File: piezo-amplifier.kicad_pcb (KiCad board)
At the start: 2 copper layers, 37 x 108 mm, 62 parts, among them J1 AudioJack4, J2 AudioJack4, J3 AudioJack4, J4 AudioJack4, J5 Conn_01x03_Male, J6 Conn_02x05_Odd_Even, SW1 734-7081, SW2 734-7081, U1 NE5532, U2 NE5532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

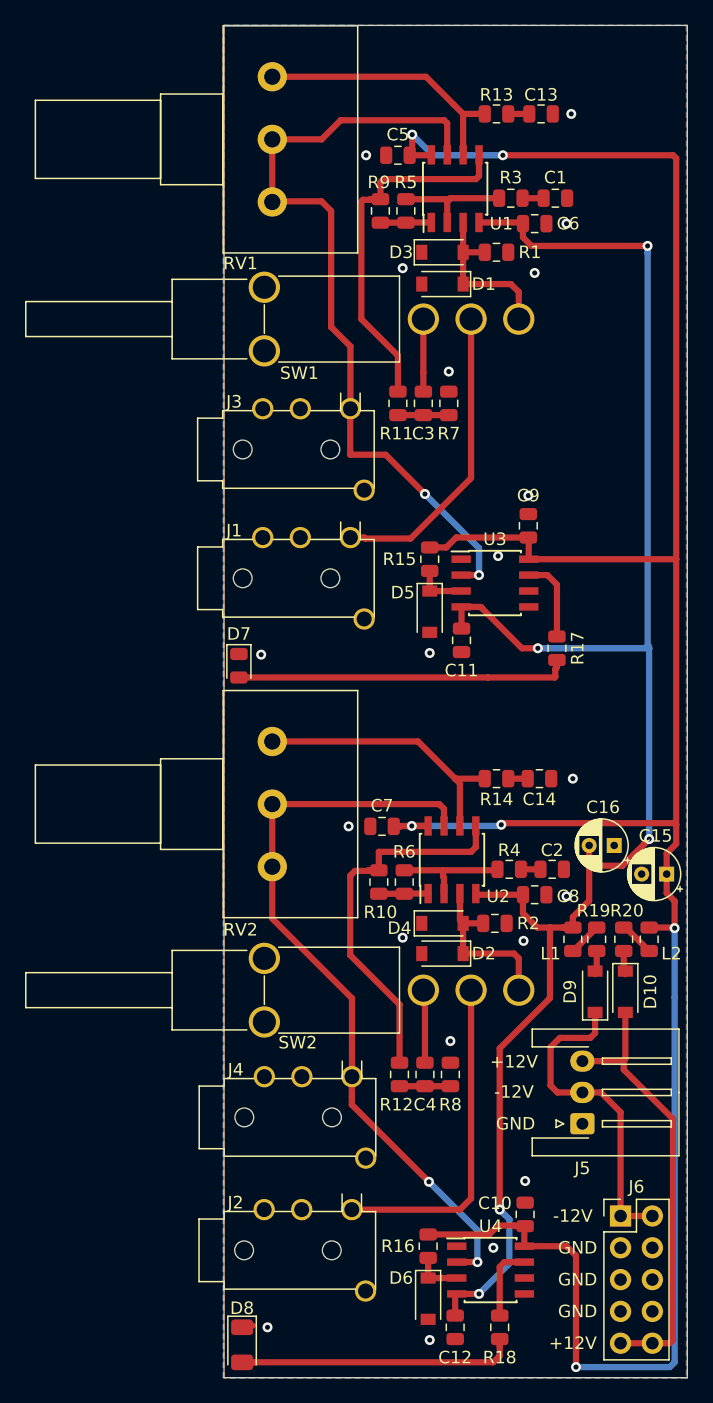
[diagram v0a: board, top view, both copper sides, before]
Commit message: switched to SMD capacitors, minor layout and silkscreen changes
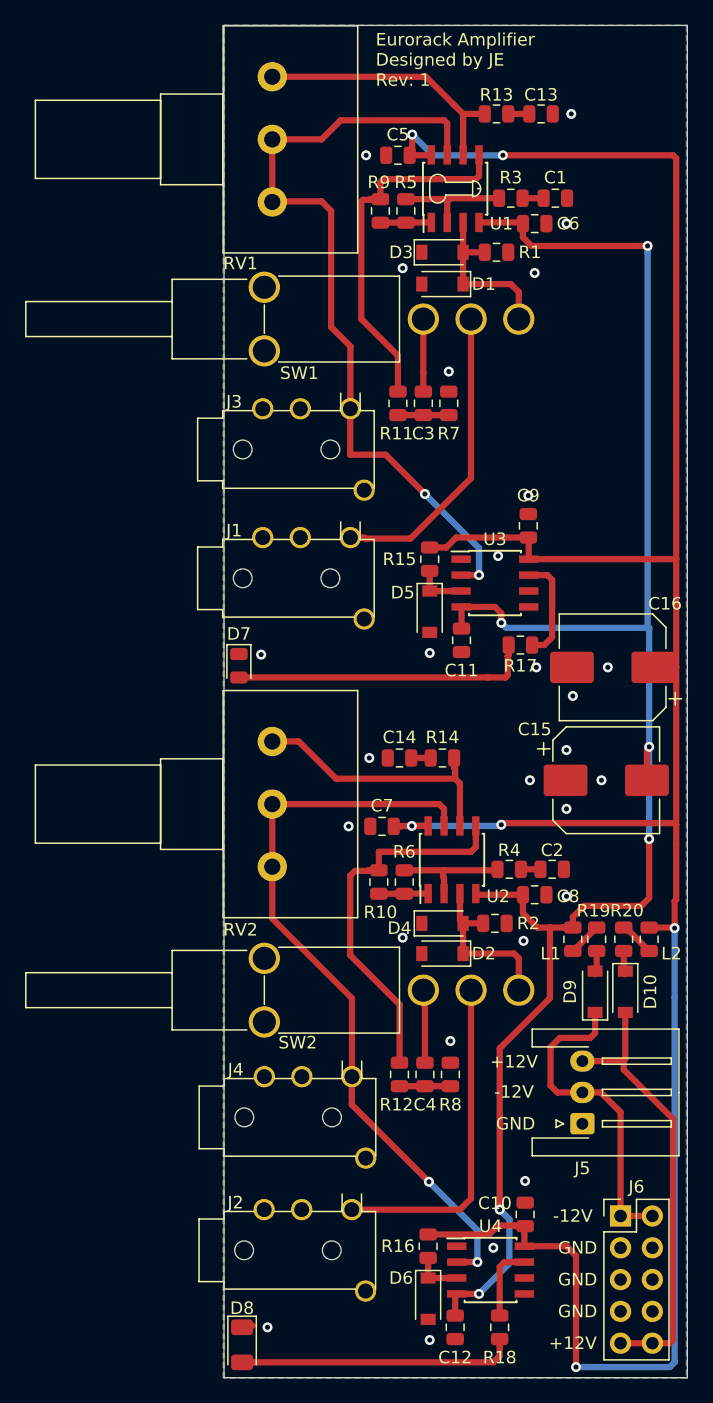
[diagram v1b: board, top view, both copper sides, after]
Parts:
- C15, C16: value 10u -> 330u; footprint Capacitor_THT:CP_Radial_D4.0mm_P2.00mm -> Capacitor_SMD:CP_Elec_8x10
- moved C15 17.1 mm to (129.0, 88.3)
- moved C14 11.3 mm to (112.0, 95.5), turned to 0 degrees
- moved C16 5.25 mm to (128.5, 97.3), turned to 0 degrees
- moved R14 4.62 mm to (115.4, 95.5), turned to 0 degrees
- moved R17 2.93 mm to (121.7, 86.5), turned to 180 degrees
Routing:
- net Net-(D7-Pad2): track 26.7 -> 24.0 mm
- net -12V: track 138.6 -> 140.9 mm, vias 5 -> 6
- net Net-(R17-Pad1): track 6.71 -> 8.47 mm
- net +12V: track 201.0 -> 202.3 mm
- net Net-(R14-Pad2): track 22.1 -> 21.5 mm
- net GND: vias 20 -> 27
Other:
- board text added: "Eurorack Amplifier Designed by JE Rev: 1"
